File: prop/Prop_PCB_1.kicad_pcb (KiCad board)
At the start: 4 copper layers, 63.5 x 63.5 mm, 18 parts, among them J1 1984989, J2 1984989, J3 1984989, J4 1984989, J5 CAS_stacking, J6 Conn_01x02, J7 1984989, U1 L298P, U1301 MAX6675ISA+, U2 SN74LVC8T245DBR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

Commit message: Done rewiring.
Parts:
- moved C2 2.85 mm to (79.5, 86.9)
- moved U1301 2.07 mm to (68.5, 82.2)
- moved C1301 1.46 mm to (79.8, 90.5)
- moved R1 1.30 mm to (79.8, 66.2), turned to -90 degrees
- moved C1 0.80 mm to (106.8, 77.8), turned to -90 degrees
- moved R2 0.59 mm to (101.8, 66.2), turned to 90 degrees
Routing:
- net +5V: track 28.7 -> 49.1 mm
- net Sol1Lead1: track 48.6 -> 57.0 mm
- net Sol1Lead2: track 50.2 -> 58.6 mm
- net Sol2: track 83.1 -> 87.2 mm
- net Sol1: track 32.7 -> 36.5 mm
- net SPI0_SCK: track 13.3 -> 16.8 mm, vias 0 -> 2
- net PWM1: track 24.0 -> 27.4 mm
- net GND: track 101.5 -> 104.9 mm, vias 28 -> 16
- net Sol2': track 42.8 -> 45.5 mm
- net PWM2: track 21.6 -> 23.8 mm
- net +3V3: track 44.9 -> 42.9 mm
- net Net-(R1-Pad2): track 2.18 -> 4.03 mm
- net +24V: track 9.71 -> 11.4 mm
- net SPI0_MISO: track 12.7 -> 14.4 mm
- net Net-(R2-Pad1): track 6.28 -> 4.69 mm
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
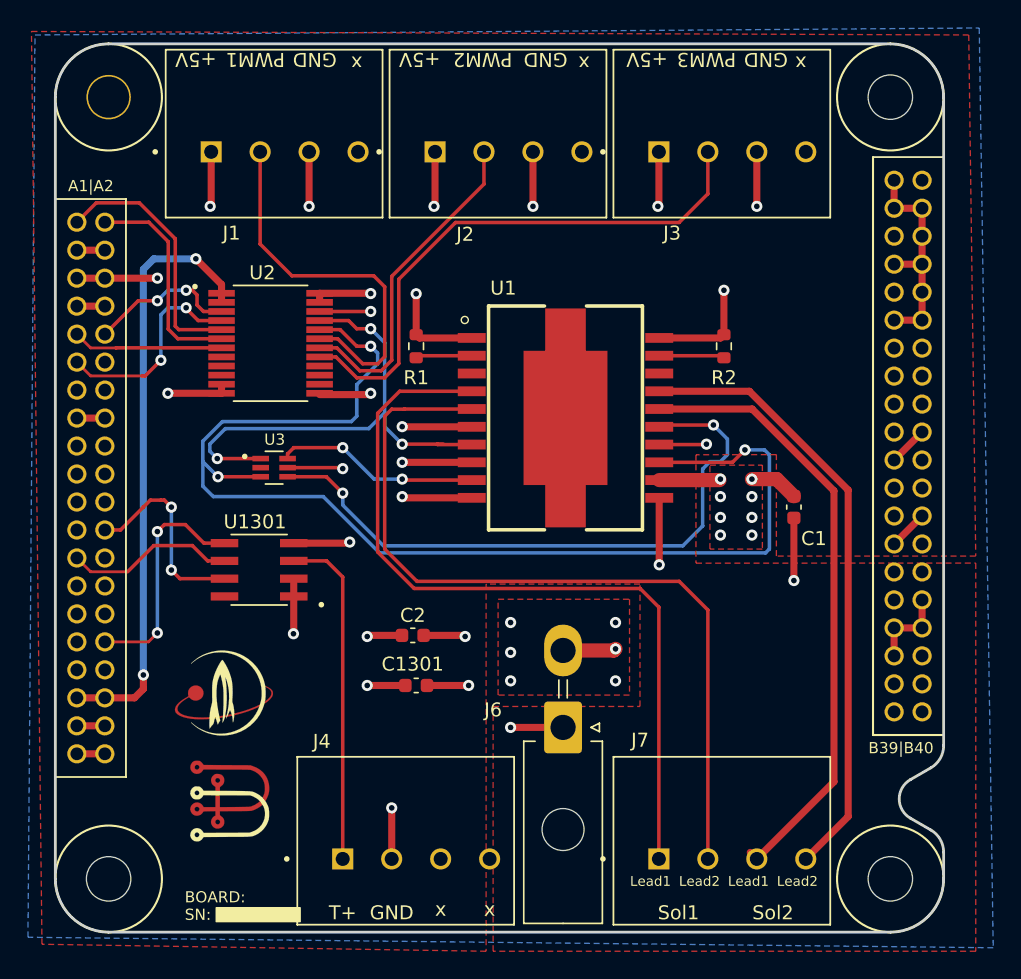
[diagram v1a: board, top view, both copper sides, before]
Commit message: Removed unconnected lines.
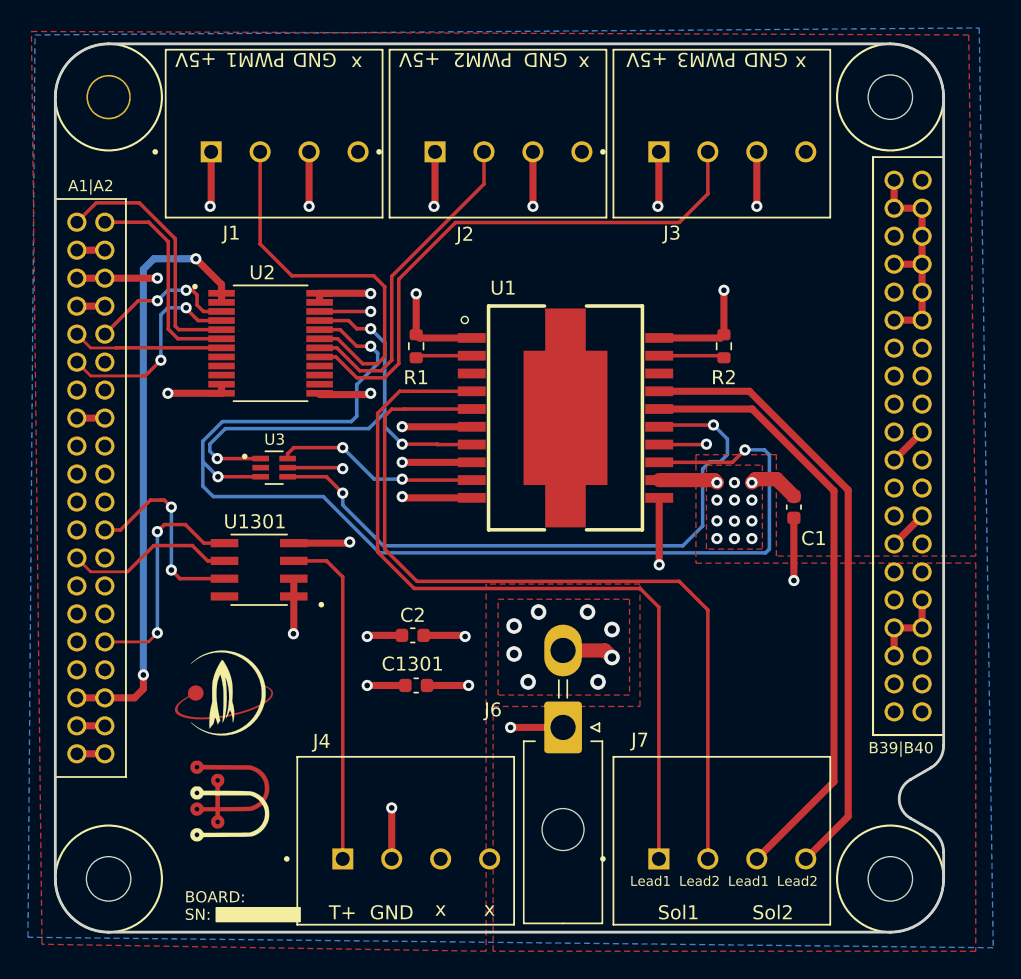
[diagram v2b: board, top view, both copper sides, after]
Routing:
- net CS4: track 12.9 -> 12.2 mm
- net Sol2Lead1: track 44.2 -> 43.5 mm
- net Sol1: track 36.5 -> 35.9 mm
- net +24V: track 11.4 -> 11.5 mm, vias 14 -> 20

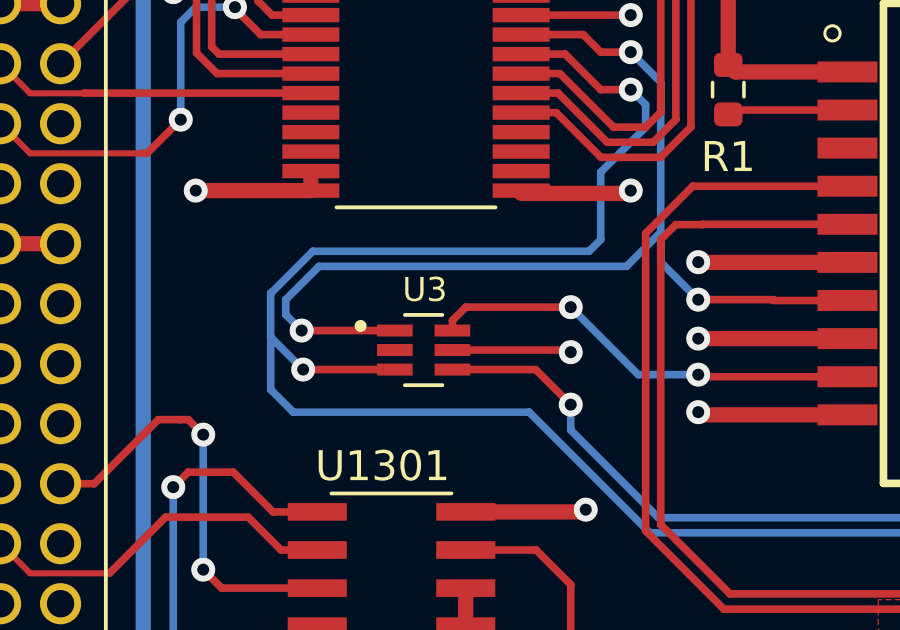
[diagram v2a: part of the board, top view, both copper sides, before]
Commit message: Fixed unconnected GND pin.
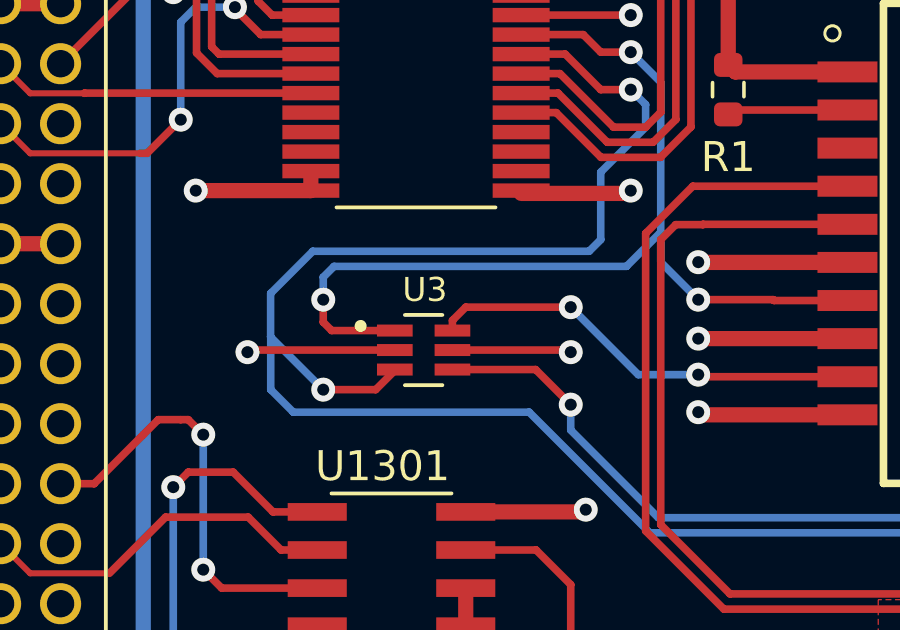
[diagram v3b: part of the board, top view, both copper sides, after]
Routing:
- net GND: track 104.9 -> 109.8 mm, vias 16 -> 17
- net Sol1: track 35.9 -> 33.9 mm
- net Sol2: track 87.2 -> 87.8 mm
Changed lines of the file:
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@@
   (segment (start 72.096 52.354) (end 72.096 56.25) (width 0.508) (layer "F.Cu") (net 1))
   (segment (start 115.915 62.385) (end 115.915 64.385) (width 0.508) (layer "F.Cu") (net 1))
-  (segment (start 97.124 65.659) (end 101.516 65.659) (width 0.508) (layer "F.Cu") (net 1))
   (segment (start 115.915 84.385) (end 115.915 86.385) (width 0.508) (layer "F.Cu") (net 1))
   (segment (start 65.837 69.615) (end 65.837 69.058511) (width 0.508) (layer "F.Cu") (net 1))
@@
   (segment (start 57.495 63.385) (end 55.495 63.385) (width 0.508) (layer "F.Cu") (net 1))
   (segment (start 115.915 64.385) (end 113.915 64.385) (width 0.508) (layer "F.Cu") (net 1))
-  (segment (start 101.516 65.659) (end 101.75 65.425) (width 0.508) (layer "F.Cu") (net 1))
   (segment (start 76.33 86.92) (end 76.25 87) (width 0.508) (layer "F.Cu") (net 1))
   (segment (start 115.915 56.3851) (end 115.915 58.3851) (width 0.508) (layer "F.Cu") (net 1))
@@
   (segment (start 72.847 63.765) (end 76.5 63.765) (width 0.254) (layer "F.Cu") (net 1))
   (segment (start 106.75 78.525) (end 106.75 83) (width 0.508) (layer "F.Cu") (net 1))
+  (segment (start 68.636 74.93) (end 63.7935 74.93) (width 0.254) (layer "F.Cu") (net 1))
+  (segment (start 63.7935 74.93) (end 63.7235 75) (width 0.254) (layer "F.Cu") (net 1))
+  (segment (start 97.124 65.659) (end 101.516 65.659) (width 0.508) (layer "F.Cu") (net 1))
+  (segment (start 101.516 65.659) (end 101.75 65.425) (width 0.508) (layer "F.Cu") (net 1))
   (segment (start 78 102.9) (end 78 99.25) (width 0.508) (layer "F.Cu") (net 1))
   (segment (start 55.495 59.385) (end 57.495 59.385) (width 0.508) (layer "F.Cu") (net 1))
@@
   (via (at 104.1 56.25) (size 0.8) (drill 0.4) (layers "F.Cu" "B.Cu") (net 1))
   (via (at 76.5 69.615) (size 0.8) (drill 0.4) (layers "F.Cu" "B.Cu") (net 1))
+  (via (at 63.7235 75) (size 0.8) (drill 0.4) (layers "F.Cu" "B.Cu") (net 1))
   (via (at 79.75 62.5) (size 0.8) (drill 0.4) (layers "F.Cu" "B.Cu") (net 1))
   (via (at 101.75 62.25) (size 0.8) (drill 0.4) (layers "F.Cu" "B.Cu") (net 1))
@@
   (segment (start 98.552 83.058) (end 100.6 85.106) (width 0.254) (layer "F.Cu") (net 11))
   (segment (start 83.724 73.279) (end 81.279 73.279) (width 0.254) (layer "F.Cu") (net 12))
-  (segment (start 68.636 74.28) (end 65.53 74.28) (width 0.254) (layer "F.Cu") (net 12))
+  (segment (start 66.25 73.5) (end 66.25 73.25) (width 0.254) (layer "F.Cu") (net 12))
   (segment (start 78.75 73.25) (end 81.25 73.25) (width 0.254) (layer "F.Cu") (net 12))
   (segment (start 74.915 64.415) (end 75.5 65) (width 0.254) (layer "F.Cu") (net 12))
+  (segment (start 66.53 74.28) (end 66.25 74) (width 0.254) (layer "F.Cu") (net 12))
+  (segment (start 66.25 74) (end 66.25 73.5) (width 0.254) (layer "F.Cu") (net 12))
   (segment (start 81.279 73.279) (end 81.25 73.25) (width 0.254) (layer "F.Cu") (net 12))
+  (segment (start 68.636 74.28) (end 66.53 74.28) (width 0.254) (layer "F.Cu") (net 12))
   (segment (start 75.5 65) (end 76.5 65) (width 0.254) (layer "F.Cu") (net 12))
   (segment (start 72.847 64.415) (end 74.915 64.415) (width 0.254) (layer "F.Cu") (net 12))
   (via (at 76.5 65) (size 0.8) (drill 0.4) (layers "F.Cu" "B.Cu") (net 12))
-  (via (at 65.53 74.28) (size 0.8) (drill 0.4) (layers "F.Cu" "B.Cu") (net 12))
+  (via (at 66.25 73.25) (size 0.8) (drill 0.4) (layers "F.Cu" "B.Cu") (net 12))
   (via (at 78.75 73.25) (size 0.8) (drill 0.4) (layers "F.Cu" "B.Cu") (net 12))
-  (segment (start 65 73.25) (end 66.109519 72.140481) (width 0.254) (layer "B.Cu") (net 12))
-  (segment (start 66.109519 72.140481) (end 76.359519 72.140481) (width 0.254) (layer "B.Cu") (net 12))
+  (segment (start 66.609519 72.140481) (end 66.25 72.5) (width 0.254) (layer "B.Cu") (net 12))
+  (segment (start 76.359519 72.140481) (end 66.609519 72.140481) (width 0.254) (layer "B.Cu") (net 12))
   (segment (start 77.5 71) (end 77.5 72) (width 0.254) (layer "B.Cu") (net 12))
+  (segment (start 77.5 71) (end 76.359519 72.140481) (width 0.254) (layer "B.Cu") (net 12))
   (segment (start 77.5 72) (end 78.75 73.25) (width 0.254) (layer "B.Cu") (net 12))
   (segment (start 77.5 66) (end 77.5 71) (width 0.254) (layer "B.Cu") (net 12))
   (segment (start 76.5 65) (end 77.5 66) (width 0.254) (layer "B.Cu") (net 12))
-  (segment (start 65.53 74.28) (end 65 73.75) (width 0.254) (layer "B.Cu") (net 12))
-  (segment (start 65 73.75) (end 65 73.25) (width 0.254) (layer "B.Cu") (net 12))
-  (segment (start 76.359519 72.140481) (end 77.5 71) (width 0.254) (layer "B.Cu") (net 12))
+  (segment (start 66.25 73.25) (end 66.25 72.5) (width 0.254) (layer "B.Cu") (net 12))
   (segment (start 71 73.5) (end 74.5 73.5) (width 0.254) (layer "F.Cu") (net 13))
   (segment (start 78.819 75.819) (end 83.724 75.819) (width 0.254) (layer "F.Cu") (net 13))
@@
   (segment (start 103.25 73.66) (end 102.361 74.549) (width 0.254) (layer "F.Cu") (net 15))
   (segment (start 75.5 66.25) (end 76.5 66.25) (width 0.254) (layer "F.Cu") (net 15))
-  (segment (start 68.636 75.58) (end 65.58 75.58) (width 0.254) (layer "F.Cu") (net 15))
+  (segment (start 68.636 75.58) (end 68.636 75.614) (width 0.254) (layer "F.Cu") (net 15))
   (segment (start 102.361 74.549) (end 97.124 74.549) (width 0.254) (layer "F.Cu") (net 15))
+  (segment (start 68.636 75.614) (end 68 76.25) (width 0.254) (layer "F.Cu") (net 15))
   (segment (start 74.315 65.065) (end 75.5 66.25) (width 0.254) (layer "F.Cu") (net 15))
   (segment (start 72.847 65.065) (end 74.315 65.065) (width 0.254) (layer "F.Cu") (net 15))
+  (segment (start 68 76.25) (end 66.25 76.25) (width 0.254) (layer "F.Cu") (net 15))
   (via (at 76.5 66.25) (size 0.8) (drill 0.4) (layers "F.Cu" "B.Cu") (net 15))
   (via (at 103.25 73.66) (size 0.8) (drill 0.4) (layers "F.Cu" "B.Cu") (net 15))
-  (via (at 65.58 75.58) (size 0.8) (drill 0.4) (layers "F.Cu" "B.Cu") (net 15))
+  (via (at 66.25 76.25) (size 0.8) (drill 0.4) (layers "F.Cu" "B.Cu") (net 15))
   (segment (start 77.135519 81.021519) (end 104.728481 81.021519) (width 0.254) (layer "B.Cu") (net 15))
   (segment (start 64.5 76.25) (end 65.25 77) (width 0.254) (layer "B.Cu") (net 15))
@@
   (segment (start 76.99648 66.74648) (end 76.5 66.25) (width 0.254) (layer "B.Cu") (net 15))
   (segment (start 104.648 73.66) (end 103.25 73.66) (width 0.254) (layer "B.Cu") (net 15))
+  (segment (start 64.49648 74.49648) (end 66.25 76.25) (width 0.254) (layer "B.Cu") (net 15))
   (segment (start 65.25 77) (end 73.114 77) (width 0.254) (layer "B.Cu") (net 15))
   (segment (start 64.496481 73.041435) (end 65.900954 71.636962) (width 0.254) (layer "B.Cu") (net 15))
   (segment (start 75.113038 71.636962) (end 75.5 71.25) (width 0.254) (layer "B.Cu") (net 15))
-  (segment (start 65.58 75.58) (end 64.49648 74.49648) (width 0.254) (layer "B.Cu") (net 15))
   (segment (start 75.5 71.25) (end 75.5 69) (width 0.254) (layer "B.Cu") (net 15))
   (segment (start 76.99648 67.50352) (end 76.99648 66.74648) (width 0.254) (layer "B.Cu") (net 15))
